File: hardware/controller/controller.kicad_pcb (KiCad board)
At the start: 4 copper layers, 80 x 100 mm, 70 parts, among them J1 TYPE-C 16PLT-H10.0, J2 TYPE-C 16PLT-H10.0, SW1 EVP-ASAC1A, SW2 CL-SB-13A-02T, SW3 EVP-ASAC1A, SW4 EVP-ASAC1A, SW5 EVP-ASAC1A, SW6 EVP-ASAC1A, U1 ZX-PM2.54-1-16PY, U10 XDJK-0051-025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

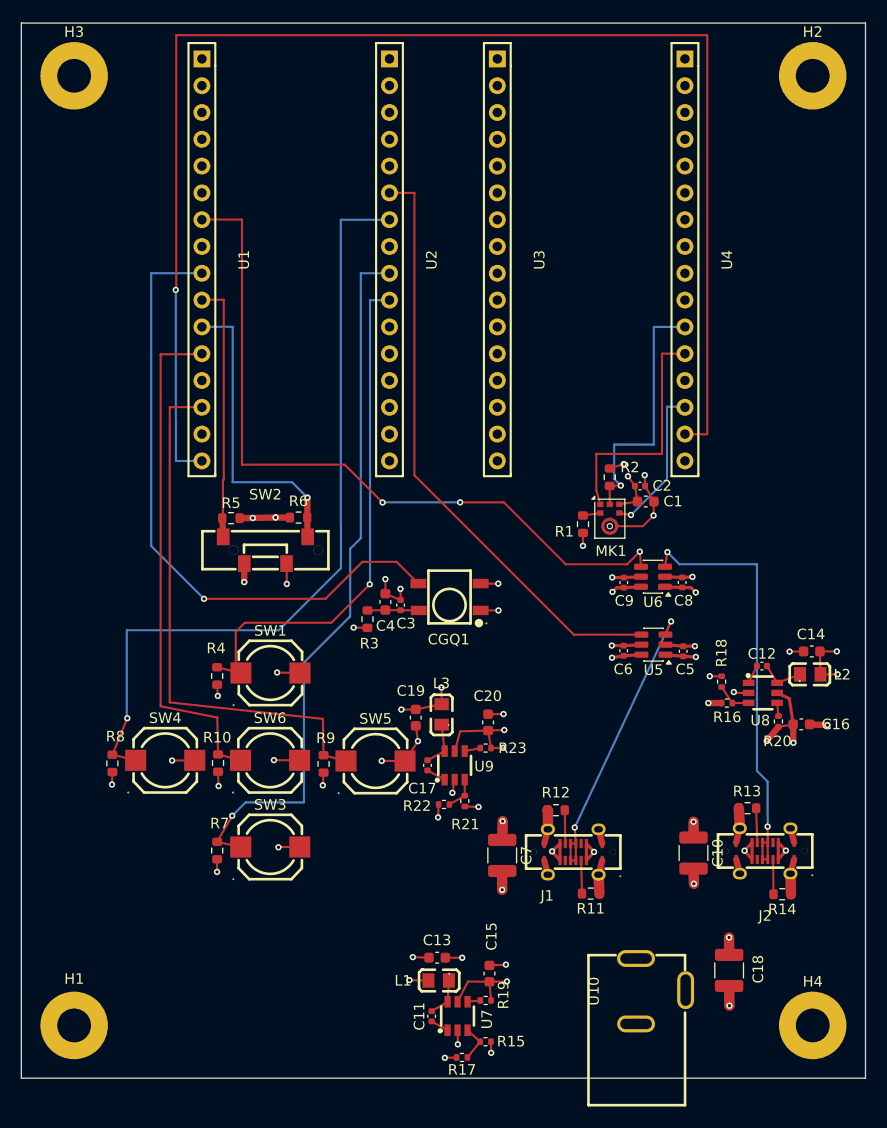
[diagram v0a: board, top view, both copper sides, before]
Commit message: rearrange the pins a bit and less insane routing
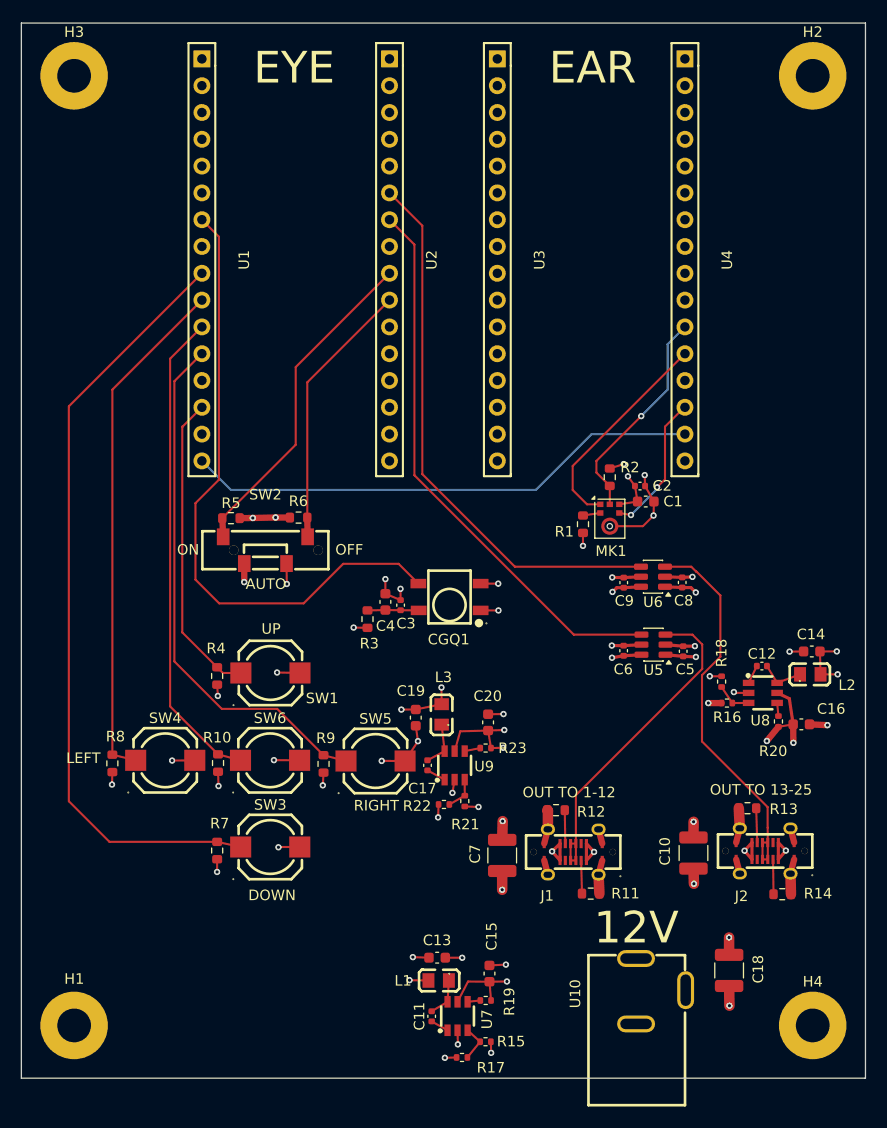
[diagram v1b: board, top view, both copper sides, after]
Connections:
- U1 pad 10: SOUND REACTIVE ON -> BTN LEFT
- U1 pad 11: SOUND REACTIVE OFF -> BTN CENTER
- U1 pad 12: BTN CENTER -> BTN RIGHT
- U1 pad 14: BTN RIGHT -> BTN UP
- U1 pad 7: LED DATA_2 -> IR SENSOR DATA
- U1 pad 9: IR SENSOR DATA -> BTN DOWN
- U2 pad 10: BTN UP -> SOUND REACTIVE OFF
- U2 pad 6: LED DATA_1 -> LED DATA_2
- U2 pad 7: BTN LEFT -> LED DATA_1
- U2 pad 9: BTN DOWN -> SOUND REACTIVE ON
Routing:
- net EAR TO EYE AUDIO: track 133.1 -> 49.1 mm, vias 1 -> 0
- net BTN LEFT: track 74.7 -> 48.9 mm, vias 1 -> 0
- net BTN UP: track 49.8 -> 29.3 mm, vias 1 -> 0
- net LED DATA_2: track 70.6 -> 52.3 mm, vias 3 -> 0
- net SOUND REACTIVE ON: track 24.6 -> 31.5 mm
- net BTN DOWN: track 67.6 -> 73.2 mm, vias 1 -> 0
- net SHIFTED_LED_DATA_2: track 41.4 -> 37.3 mm, vias 2 -> 0
- net MIC DATA OUTPUT: track 24.8 -> 20.8 mm
- net LED DATA_1: track 56.9 -> 53.0 mm
- net SOUND REACTIVE OFF: track 29.1 -> 25.7 mm, vias 1 -> 0
- net SHIFTED_LED_DATA_1: track 28.6 -> 31.9 mm, vias 2 -> 0
- net BTN CENTER: track 48.5 -> 45.8 mm
- net MIC WS: track 22.7 -> 20.5 mm
- net MIC CLOCK: track 14.5 -> 13.4 mm, vias 1 -> 2
- net BTN RIGHT: track 51.3 -> 50.3 mm
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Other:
- board text added: "12V"
- board text added: "AUTO"
- board text added: "DOWN"
- board text added: "EAR"
- board text added: "EYE"
- board text added: "LEFT"
- board text added: "OFF"
- board text added: "ON"
- board text added: "OUT TO 1-12"
- board text added: "OUT TO 13-25"
- board text added: "RIGHT"
- board text added: "UP"

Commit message: controller layout updates
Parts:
- moved R16 0.55 mm to (175.4, 120.0)
- moved R18 0.55 mm to (174.9, 118.0)
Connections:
- U3 pad 15: unconnected-(U3-Pad15) -> EAR TO EYE AUDIO
- U3 pad 16: GND -> unconnected-(U3-Pad16)
- U3 pad 2: +5V -> unconnected-(U3-Pad2)
- U4 pad 10: unconnected-(U4-Pad10) -> MIC DATA OUTPUT
- U4 pad 11: MIC DATA OUTPUT -> unconnected-(U4-Pad11)
- U4 pad 12: MIC WS -> MIC CLOCK
- U4 pad 14: MIC CLOCK -> unconnected-(U4-Pad14)
- U4 pad 15: EAR TO EYE AUDIO -> unconnected-(U4-Pad15)
- U4 pad 16: unconnected-(U4-Pad16) -> GND
- U4 pad 2: unconnected-(U4-Pad2) -> +5V
- U4 pad 9: unconnected-(U4-Pad9) -> MIC WS
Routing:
- net EAR TO EYE AUDIO: track 49.1 -> 36.0 mm
- net MIC CLOCK: track 13.4 -> 23.3 mm, vias 2 -> 0
- net MIC WS: track 20.5 -> 27.2 mm
- net MIC DATA OUTPUT: track 20.8 -> 23.4 mm, vias 1 -> 0
- net GND: track 89.2 -> 86.8 mm, vias 35 -> 36
- net +12V: track 45.1 -> 45.9 mm
- net SHIFTED_LED_DATA_1: track 31.9 -> 32.5 mm
